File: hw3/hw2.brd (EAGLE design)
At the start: 50 x 50 mm, 22 parts, among them J1 USB-MB-H

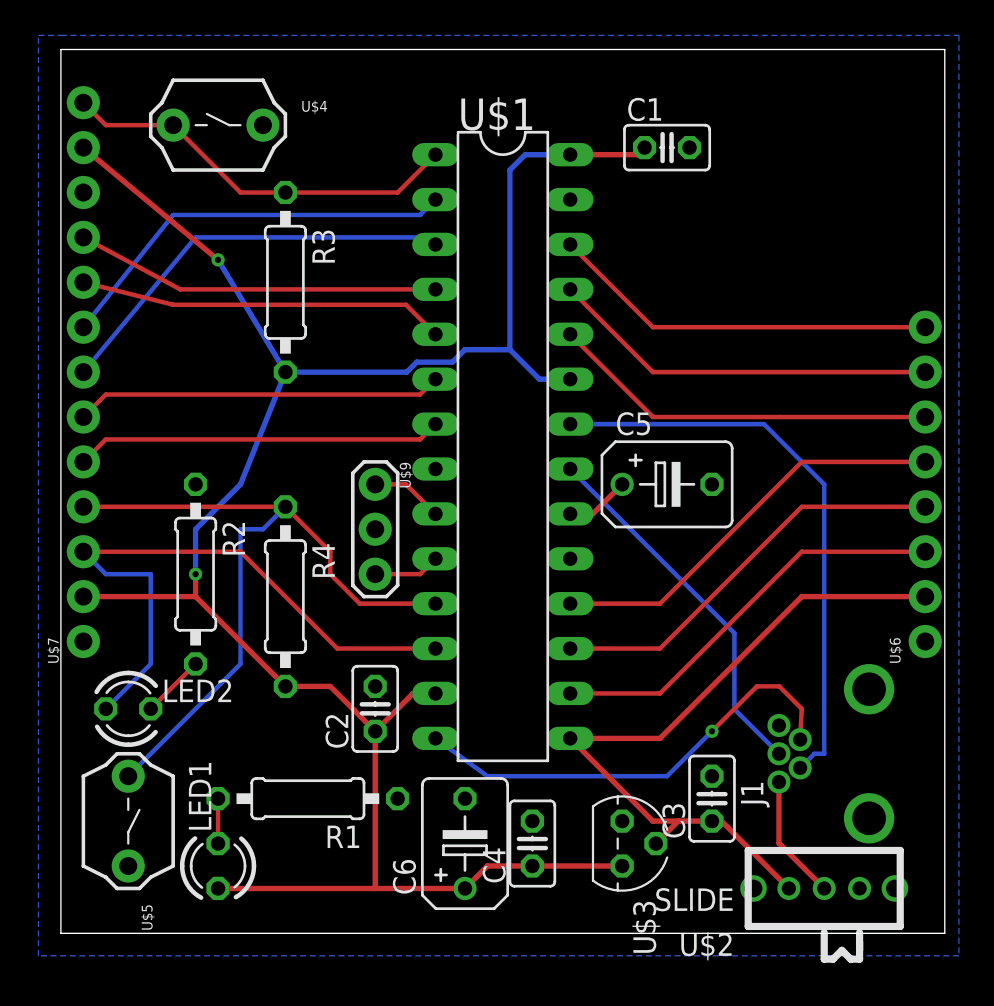
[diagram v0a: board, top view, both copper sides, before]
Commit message: completed layout and created zip file
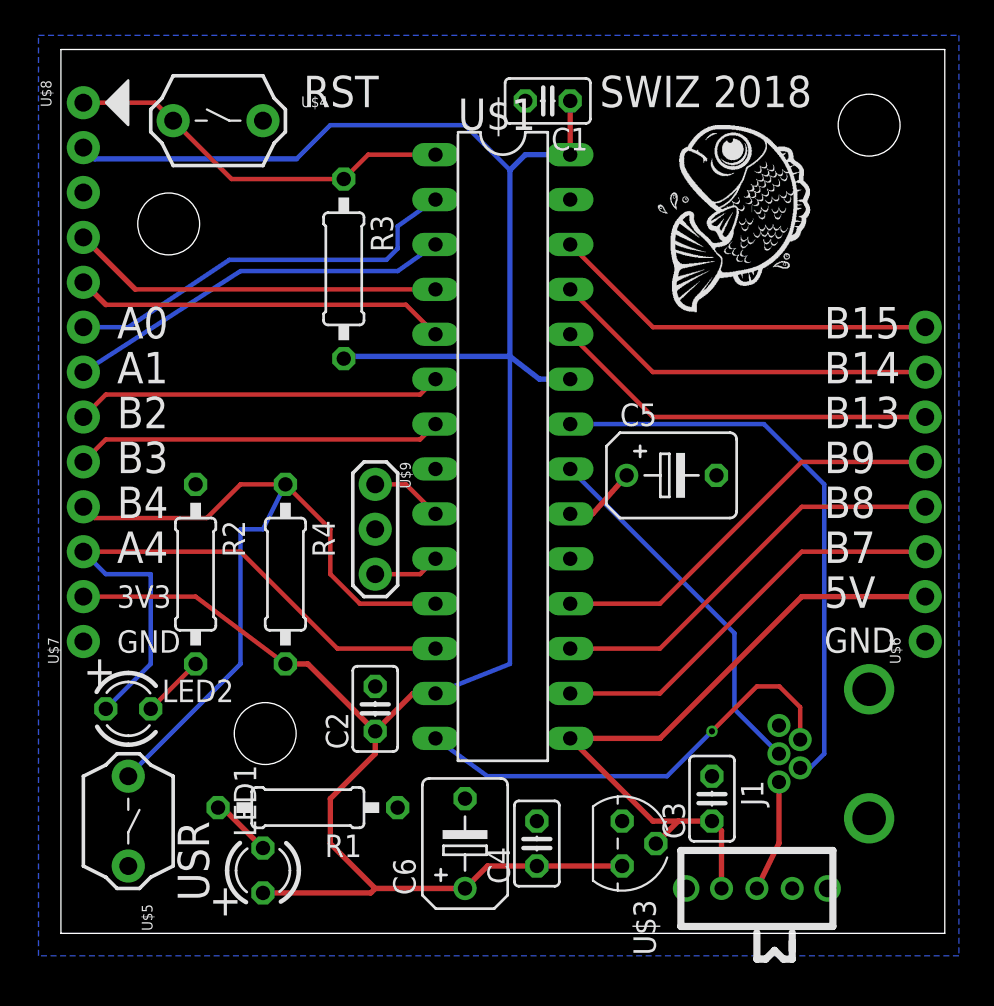
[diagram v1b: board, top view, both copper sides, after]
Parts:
- moved C1 7.25 mm to (27.5, 47.1), turned to 180 degrees
- moved U$2 3.81 mm to (39.4, 2.54)
- moved R3 3.39 mm to (16.0, 37.6)
- moved LED1 2.55 mm to (11.4, 3.56)
- moved R4 1.27 mm to (12.7, 20.3)
- moved C5 0.57 mm to (34.5, 25.9)
- moved R1 0.51 mm to (14.0, 7.11)
- moved C4 0.25 mm to (26.9, 5.08)
- moved U$4 0.25 mm to (8.89, 46.0)
- flipped U$8 to the top
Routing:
- net +3V3: track 123.4 -> 134.4 mm, vias 2 -> 0
- net B4/USER: track 42.6 -> 46.0 mm
- net +5V: track 41.0 -> 39.2 mm
- net A1: track 23.6 -> 22.1 mm
- net N$4: track 2.54 -> 3.49 mm
- net N$1: track 7.08 -> 6.31 mm
- net MCLR: track 22.9 -> 22.3 mm
- net N$6: track 3.63 -> 4.18 mm
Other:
- board text added: "+"
- board text added: "3V3"
- board text added: "5V"
- board text added: "A0"
- board text added: "A1"
- board text added: "A4"
- board text added: "B13"
- board text added: "B14"
- board text added: "B15"
- board text added: "B2"
- board text added: "B3"
- board text added: "B4"
- board text added: "B7"
- board text added: "B8"
- board text added: "B9"
- board text added: "GND"
- board text added: "RST"
- board text added: "SWIZ 2018"
- board text added: "USR"
